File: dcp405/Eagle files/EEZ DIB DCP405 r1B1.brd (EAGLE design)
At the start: 185 x 95 mm, 319 parts, among them IC1 LTC3864EMSE#PBF, IC10 MC33272ADR2G, IC11 MC33274ADR2G, IC12 LTC2050HVCS8#PBF, IC13 74AUP1G74DC.125, IC14 MCP23S17-E/SS, IC15 REF5025AIDR, IC16 DAC8552IDGKR, IC17 SN74LVC1G3157DCKR, IC18 ADS1120IPWR, IC19 LM339D, IC2 TL783CKCSE3, IC20 MAX9141ESA, IC3 LP2951SO8, IC4 SI8641BB-B-IS1, IC5 SN74LVC1G139DCUR, IC6 LTC3260EMSE#PBF, IC7 SI8641BB-B-IS1, IC8 M24C32-WMN6P, IC9 TMP1075AIDGK, J1 4907, J2 FCR7350R, J3 FCR7350B, K1 G6K-2F-5DC, Q1 IRFR5305, Q10 MMBT5551, Q11 MMBT5551, Q12 PSMN0R9-25YLC, Q13 PSMN0R9-25YLC, Q14 PSMN0R9-25YLC, Q15 2N7002, Q16 BSS84P, Q17 BTA26-600, Q18 FMMT493TA, Q19 2N7002, Q2 MMBT5401, Q20 2N7002, Q21 2N7002, Q22 MMBT5551, Q23 MMBT5401, Q24 MMBT5551, Q25 MMBT5551, Q26 2N7002, Q3 IRFP250MPBF, Q4 BC856C, Q5 BCP56-16.115, Q6 STF10P6F6, Q7 BCP56-16.115, Q8 MMBT5401, Q9 MMBT5401, X1 172648-0102, X2 M20-9701346, X3 1844249, X4 ZL263-20DG

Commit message: DCP405 BOM
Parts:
- IC11: value MC33274ADR2G -> MC33272ADR2G
- IC3: value LP2951SO8 -> LP2951
- KK1, KK2: value PCB-MB -> PCB-MB-01
- L1: value RN112-4-02 -> RN112-4-02-0M7
- Q1: value IRFR5305 -> SUD19P06-60
- R71: value 0R010 -> 0R010 (low TCR)
- X1: value 172648-0102 -> 39-30-1020
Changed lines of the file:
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@@
 <attribute name="VALUE" x="131.5585" y="47.4655" size="1.016" layer="27" ratio="10" rot="R180"/>
 </element>
-<element name="IC11" library="EEZ_Lib1" package="SOIC127P600X173-8N" value="MC33274ADR2G" x="85.6615" y="24.257" smashed="yes" rot="R180">
+<element name="IC11" library="EEZ_Lib1" package="SOIC127P600X173-8N" value="MC33272ADR2G" x="85.6615" y="24.257" smashed="yes" rot="R180">
 <attribute name="NAME" x="90.4875" y="24.5491" size="1.016" layer="25" ratio="10" rot="SR90"/>
 <attribute name="VALUE" x="82.3436" y="24.049" size="0.6096" layer="27" ratio="10" rot="SR0"/>
@@
 <attribute name="VALUE" x="27.305" y="55.5625" size="1.016" layer="27" ratio="10" rot="R90"/>
 </element>
-<element name="KK1" library="EEZ_Lib1" package="PCB-MB" value="PCB-MB" x="11" y="89.5" smashed="yes"/>
-<element name="KK2" library="EEZ_Lib1" package="PCB-MB" value="PCB-MB" x="11" y="5.5" smashed="yes"/>
+<element name="KK1" library="EEZ_Lib1" package="PCB-MB" value="PCB-MB-01" x="11" y="89.5" smashed="yes"/>
+<element name="KK2" library="EEZ_Lib1" package="PCB-MB" value="PCB-MB-01" x="11" y="5.5" smashed="yes"/>
 <element name="C37" library="rcl" package="C0603" value="100n" x="89.0905" y="5.207" smashed="yes" rot="R270">
 <attribute name="NAME" x="87.63" y="7.0485" size="1.016" layer="25" ratio="10"/>
@@
 <attribute name="VALUE" x="110.4265" y="5.1435" size="0.8128" layer="27" ratio="10" rot="R90"/>
 </element>
-<element name="X1" library="EEZ_connectors" package="MINIFIT_39301020" value="172648-0102" x="171.069" y="10.6045" smashed="yes" rot="R90">
+<element name="X1" library="EEZ_connectors" package="MINIFIT_39301020" value="39-30-1020" x="171.069" y="10.6045" smashed="yes" rot="R90">
 <attribute name="NAME" x="177.7135" y="13.59" size="1.27" layer="25" ratio="10"/>
 <attribute name="VALUE" x="171.943" y="10.105" size="1.27" layer="27" ratio="10"/>
@@
 <attribute name="NAME" x="180.4035" y="75.8825" size="0.6096" layer="52" rot="R270"/>
 </element>
-<element name="Q1" library="EEZ_Lib1" package="TO229P990X239-3N" value="IRFR5305" x="158.3055" y="49.911" smashed="yes" rot="R90">
+<element name="Q1" library="EEZ_Lib1" package="TO229P990X239-3N" value="SUD19P06-60" x="158.3055" y="49.911" smashed="yes" rot="R90">
 <attribute name="NAME" x="154.8765" y="50.546" size="1.27" layer="25" ratio="10" rot="R180"/>
 <attribute name="VALUE" x="161.4805" y="50.4825" size="1.016" layer="27" ratio="10" rot="R180"/>
@@
 <attribute name="VALUE" x="146.8755" y="38.608" size="1.016" layer="27" ratio="10" rot="R270"/>
 </element>
-<element name="IC3" library="EEZ_Lib1" package="SOIC127P600X175-8N" value="LP2951SO8" x="152.527" y="37.0205" smashed="yes">
+<element name="IC3" library="EEZ_Lib1" package="SOIC127P600X175-8N" value="LP2951" x="152.527" y="37.0205" smashed="yes">
 <attribute name="NAME" x="151.1681" y="33.0835" size="1.27" layer="25" ratio="10" rot="SR0"/>
 <attribute name="VALUE" x="148.3106" y="36.576" size="1.016" layer="27" ratio="10" rot="SR0"/>
@@
 <attribute name="VALUE" x="156.9065" y="32.718" size="0.8128" layer="27" ratio="10" rot="R270"/>
 </element>
-<element name="L1" library="EEZ_Lib1" package="RN112" value="RN112-4-02" x="172.0215" y="23.622" smashed="yes" rot="R180">
+<element name="L1" library="EEZ_Lib1" package="RN112" value="RN112-4-02-0M7" x="172.0215" y="23.622" smashed="yes" rot="R180">
 <attribute name="NAME" x="163.1442" y="31.3817" size="1.6764" layer="25" ratio="10"/>
 <attribute name="VALUE" x="164.0302" y="22.9597" size="1.6764" layer="27"/>
@@
 <attribute name="VALUE" x="48.895" y="86.5505" size="1.27" layer="27"/>
 </element>
-<element name="R71" library="EEZ_Lib1" package="R_H2728" value="0R010" x="75.5015" y="71.8185" smashed="yes" rot="R180">
+<element name="R71" library="EEZ_Lib1" package="R_H2728" value="0R010 (low TCR)" x="75.5015" y="71.8185" smashed="yes" rot="R180">
 <attribute name="NAME" x="80.391" y="71.1835" size="1.27" layer="25" ratio="10"/>
 <attribute name="VALUE" x="75.5015" y="71.8185" size="1.27" layer="27" rot="R180" align="center"/>

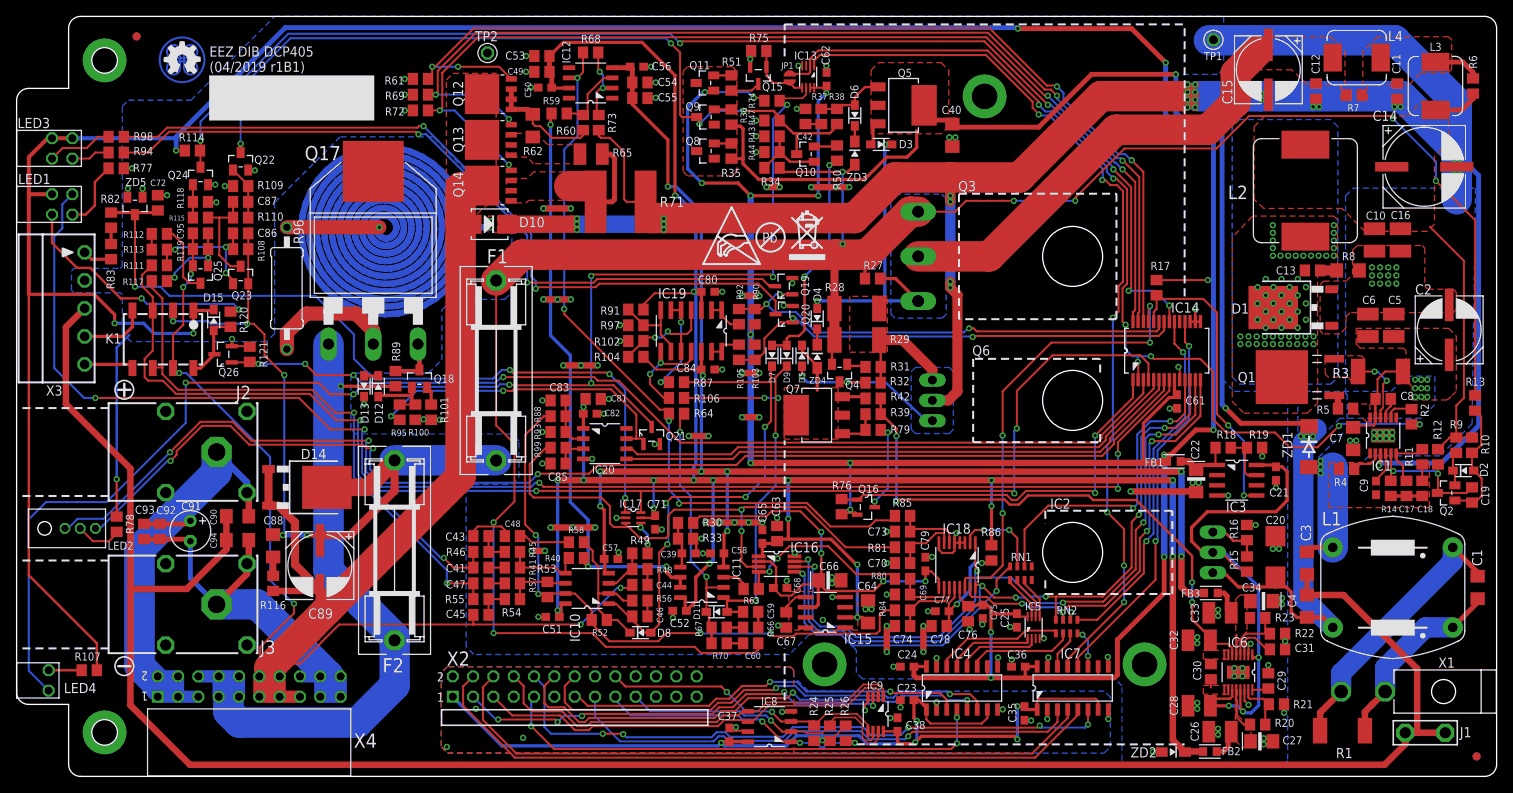
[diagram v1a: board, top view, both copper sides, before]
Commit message: DCP405 BOM update, JP2 added
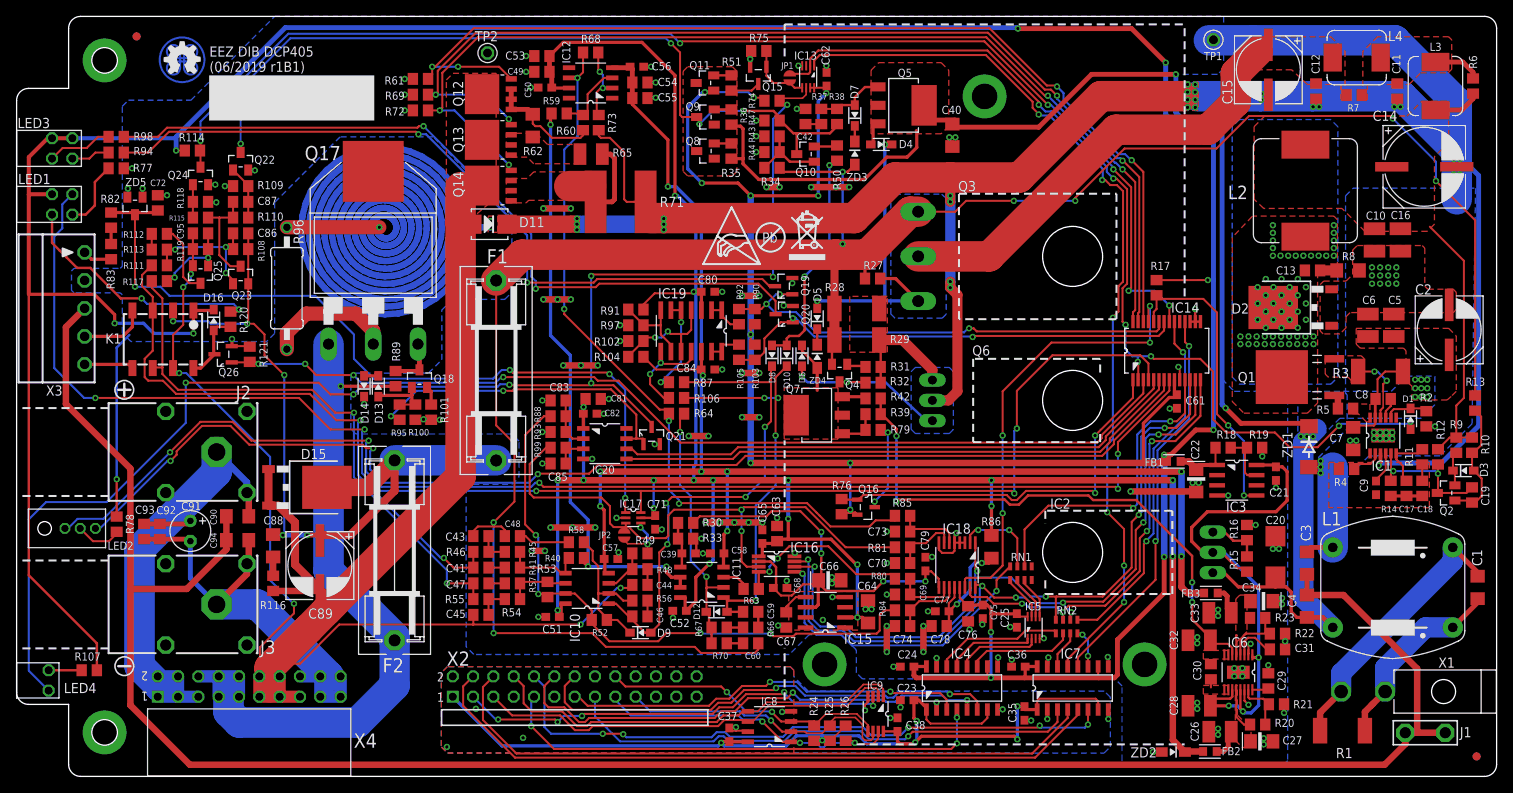
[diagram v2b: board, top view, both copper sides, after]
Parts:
- added D16: BAS316, EEZ_Lib1:SOD323-R
- added JP2: JP2-CUT, EEZ_Lib1:JP2-CUT
- C22, C66: value 4u7 -> 4u7 tant.
- C27, C34: value 10u -> 10u tant.
- D1: value STPS15H100 -> BAS316; device EEZ_Lib1:TO252-L -> EEZ_Lib1:SOD323-R
- D10: value SK55 -> BAS316; device EEZ_Lib1:SMB -> EEZ_Lib1:SOD323-R
- D11: value BAS316 -> SK55; device EEZ_Lib1:SOD323-R -> EEZ_Lib1:SMB
- D14: value SK10100D1-DIO -> BAS316; device EEZ_Lib1:TO252-L -> EEZ_Lib1:SOD323-R
- D15: value BAS316 -> SK10100D1-DIO; device EEZ_Lib1:SOD323-R -> EEZ_Lib1:TO252-L
- D2: value BAS316 -> STPS15H100; device EEZ_Lib1:SOD323-R -> EEZ_Lib1:TO252-L
- IC10: value MC33272ADR2G -> OPA2196ID
- R86: device rcl:R0805 -> rcl:R1206
- moved D3 83.4 mm to (180.8, 38.2), turned to 0 degrees
- moved D11 56.2 mm to (59.1, 69.0), turned to 180 degrees
- moved D12 50.8 mm to (87.5, 20.6), turned to 0 degrees
- moved D10 40.6 mm to (96.3, 52.6), turned to 90 degrees
- moved D9 39.1 mm to (78.0, 18.0), turned to 0 degrees
- moved D8 38.3 mm to (94.4, 52.6), turned to 90 degrees
- moved D7 31.8 mm to (104.8, 82.6)
- moved D6 30.8 mm to (98.2, 52.6), turned to 270 degrees
- moved D2 30.4 mm to (158.3, 58.6), turned to 90 degrees
- moved D15 24.6 mm to (37.6, 36.1)
- moved D4 23.2 mm to (108.1, 79.0), turned to 180 degrees
- moved D1 21.2 mm to (174.2, 44.7), turned to 270 degrees
- moved D14 13.9 mm to (43.4, 48.8), turned to 90 degrees
- moved D5 5.01 mm to (100.1, 57.2), turned to 90 degrees
- moved R2 1.86 mm to (176.2, 44.7), turned to 90 degrees
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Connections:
- removed net N$36: IC1.8, R2.1
- new net N$7: D1.C, IC1.8, R2.2
- net +5V: now also D16.C; no longer D15.C
- net GND: now also D14.C; no longer D13.C
- net I_SERVO: now also D10.C, D12.A; no longer D11.A, D9.C
- net LOOP_CTRL: now also D10.A, D8.A; no longer D7.A, D9.A
- net N$1: now also D3.C; no longer D2.C
- net N$114: now also D16.A; no longer D15.A
- net N$129: now also D7.C; no longer D6.C
- net N$143: now also D5.C; no longer D4.C
- net N$147: now also D6.A; no longer D5.A
- net N$20: now also D13.C, D14.A; no longer D12.C, D13.A
- net N$21: now also D13.A; no longer D12.A
- net N$79: now also D3.A; no longer D2.A
- net N$84: now also D9.C; no longer D8.C
- net N$89: now also D12.C; no longer D11.C
- net N$92: now also D4.C, D5.A; no longer D3.C, D4.A
- net N$93: now also D4.A; no longer D3.A
- net N$95: now also D7.A; no longer D6.A
- net POST_OUT-: now also D11.A, D15.1, D15.2; no longer D10.A, D14.1, D14.2
- net POST_OUTF+: now also D15.3; no longer D14.3
- net PREG_IN-: now also D2.1, D2.2, R2.1; no longer D1.1, D1.2
- net PREG_OUT-: now also D11.C; no longer D10.C
- net PRE_OE: now also D1.A; no longer R2.2
- net Q6C: now also D6.C; no longer D5.C
- net SW: now also D2.3; no longer D1.3
- net U_SERVO: now also D8.C, D9.A; no longer D7.C, D8.A
- net U_SET: now also JP2.1
- net U_SET_OUT: now also JP2.2
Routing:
- net N$7: track 0.00 -> 5.46 mm
- net N$36: track 3.47 -> 0.00 mm
- net U_SET_OUT: track 4.17 -> 7.31 mm
- net V+: track 302.2 -> 301.0 mm
- net PRE_OE: track 123.2 -> 122.0 mm
- net PREG_IN-: track 62.0 -> 63.1 mm, vias 29 -> 30
- net U_SET: track 71.3 -> 72.0 mm
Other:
- board text added: "EEZ DIB DCP405 (06/2019 r1B1)"
- board text added: "EEZ DIB DCP405 (06/2019 r1B1) DC power source 0-40V / 50mA-500mA-5A Project source code: github.com/eez-open"
- board text removed: "EEZ DIB DCP405 (04/2019 r1B1)"
- board text removed: "EEZ DIB DCP405 (04/2019 r1B1) DC power source 0-40V / 50mA-500mA-5A Project source code: github.com/eez-open"
